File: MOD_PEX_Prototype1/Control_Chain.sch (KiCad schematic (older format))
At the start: 25 parts, among them J1 RJ45_CHAIN_MAIN, J2 RJ45_CHAIN_EXTENSION, Q1 MMBT3904, Q2 MMBT3906, U4 MAX13450E

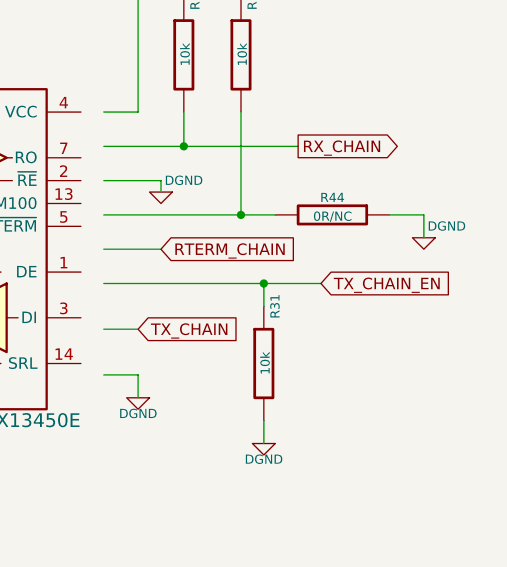
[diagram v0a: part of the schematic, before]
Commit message: Fixing control chain signal names, adding a 0R resistor for the ENABLE_CHAIN signal in the P1 debugging connector and regenerating the netlist.
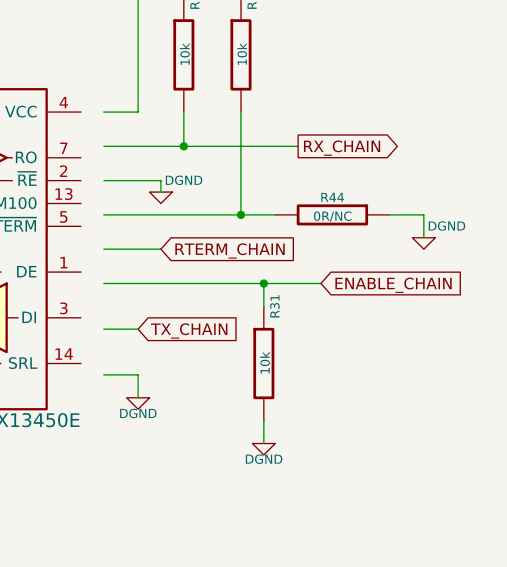
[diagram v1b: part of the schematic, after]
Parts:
- Q1: footprint (none) -> MOD_Footprints_Lib:SOT23
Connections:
- net labels added: ENABLE_CHAIN
- net labels removed: TX_CHAIN_EN
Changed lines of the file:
@@
 $EndComp
 $Comp
-L +3.3V #PWR25
+L +3.3V #PWR028
 U 1 1 548B5A42
 P 1900 2050
-F 0 "#PWR25" H 1900 2010 30  0001 C CNN
+F 0 "#PWR028" H 1900 2010 30  0001 C CNN
 F 1 "+3.3V" H 1900 2160 30  0000 C CNN
 F 2 "" H 1900 2050 60  0000 C CNN
@@
 $EndComp
 $Comp
-L DGND #PWR26
+L DGND #PWR029
 U 1 1 548B5A48
 P 2200 5950
-F 0 "#PWR26" H 2200 5950 40  0001 C CNN
+F 0 "#PWR029" H 2200 5950 40  0001 C CNN
 F 1 "DGND" H 2200 5880 40  0000 C CNN
 F 2 "" H 2200 5950 60  0000 C CNN
@@
 $EndComp
 $Comp
-L DGND #PWR28
+L DGND #PWR030
 U 1 1 548B5A55
 P 2350 4800
-F 0 "#PWR28" H 2350 4800 40  0001 C CNN
+F 0 "#PWR030" H 2350 4800 40  0001 C CNN
 F 1 "DGND" H 2350 4730 40  0000 C CNN
 F 2 "" H 2350 4800 60  0000 C CNN
@@
 RS485_RX-
 $Comp
-L DGND #PWR37
+L DGND #PWR031
 U 1 1 548B5A5E
 P 7250 3250
-F 0 "#PWR37" H 7250 3250 40  0001 C CNN
+F 0 "#PWR031" H 7250 3250 40  0001 C CNN
 F 1 "DGND" H 7250 3150 40  0000 C CNN
 F 2 "" H 7250 3250 60  0000 C CNN
@@
 RX_CHAIN
 Text GLabel 9750 3300 2    50   Input ~ 0
-TX_CHAIN_EN
+ENABLE_CHAIN
 $Comp
 L ZENERsmall D3
@@
 $EndComp
 $Comp
-L DGND #PWR39
+L DGND #PWR032
 U 1 1 548B5A8A
 P 8100 4200
-F 0 "#PWR39" H 8100 4200 40  0001 C CNN
+F 0 "#PWR032" H 8100 4200 40  0001 C CNN
 F 1 "DGND" H 8100 4130 40  0000 C CNN
 F 2 "" H 8100 4200 60  0000 C CNN
@@
 $EndComp
 $Comp
-L DGND #PWR38
+L DGND #PWR033
 U 1 1 548B5A97
 P 7950 5000
-F 0 "#PWR38" H 7950 5000 40  0001 C CNN
+F 0 "#PWR033" H 7950 5000 40  0001 C CNN
 F 1 "DGND" H 7950 4930 40  0000 C CNN
 F 2 "" H 7950 5000 60  0000 C CNN
@@
 PCB consideration: \nThis capacitor must \nbe placed as close as \npossible to the IC
 $Comp
-L +5V #PWR40
+L +5V #PWR034
 U 1 1 548B5A9E
 P 8950 1900
-F 0 "#PWR40" H 8950 1990 20  0001 C CNN
+F 0 "#PWR034" H 8950 1990 20  0001 C CNN
 F 1 "+5V" H 8950 1990 30  0000 C CNN
 F 2 "" H 8950 1900 60  0000 C CNN
@@
 $EndComp
 $Comp
-L DGND #PWR41
+L DGND #PWR035
 U 1 1 548B5AA4
 P 8950 3800
-F 0 "#PWR41" H 8950 3800 40  0001 C CNN
+F 0 "#PWR035" H 8950 3800 40  0001 C CNN
 F 1 "DGND" H 8950 3730 40  0000 C CNN
 F 2 "" H 8950 3800 60  0000 C CNN
@@
 $EndComp
 $Comp
-L DGND #PWR43
+L DGND #PWR036
 U 1 1 548B5AAA
 P 9500 4000
-F 0 "#PWR43" H 9500 4000 40  0001 C CNN
+F 0 "#PWR036" H 9500 4000 40  0001 C CNN
 F 1 "DGND" H 9500 3930 40  0000 C CNN
 F 2 "" H 9500 4000 60  0000 C CNN
@@
 $EndComp
 $Comp
-L DGND #PWR42
+L DGND #PWR037
 U 1 1 548B5AB0
 P 9050 2900
-F 0 "#PWR42" H 9050 2900 40  0001 C CNN
+F 0 "#PWR037" H 9050 2900 40  0001 C CNN
 F 1 "DGND" H 8950 2950 40  0000 C CNN
 F 2 "" H 9050 2900 60  0000 C CNN
@@
 RS485_TX-
 $Comp
-L DGND #PWR27
+L DGND #PWR038
 U 1 1 548B5ABF
 P 2350 3050
-F 0 "#PWR27" H 2350 3050 40  0001 C CNN
+F 0 "#PWR038" H 2350 3050 40  0001 C CNN
 F 1 "DGND" H 2350 2980 40  0000 C CNN
 F 2 "" H 2350 3050 60  0000 C CNN
@@
 $EndComp
 $Comp
-L DGND #PWR44
+L DGND #PWR039
 U 1 1 548B5ACC
 P 10200 3100
-F 0 "#PWR44" H 10200 3100 40  0001 C CNN
+F 0 "#PWR039" H 10200 3100 40  0001 C CNN
 F 1 "DGND" H 10100 3150 40  0000 C CNN
 F 2 "" H 10200 3100 60  0000 C CNN
@@
 RS485_RX-
 $Comp
-L VCC #PWR29
+L VCC #PWR040
 U 1 1 548B5AD6
 P 3600 2450
-F 0 "#PWR29" H 3600 2550 30  0001 C CNN
+F 0 "#PWR040" H 3600 2550 30  0001 C CNN
 F 1 "VCC" H 3600 2550 30  0000 C CNN
 F 2 "" H 3600 2450 60  0000 C CNN
@@
 $EndComp
 $Comp
-L DGND #PWR31
+L DGND #PWR041
 U 1 1 548B5ADC
 P 3600 5950
-F 0 "#PWR31" H 3600 5950 40  0001 C CNN
+F 0 "#PWR041" H 3600 5950 40  0001 C CNN
 F 1 "DGND" H 3600 5880 40  0000 C CNN
 F 2 "" H 3600 5950 60  0000 C CNN
@@
 $EndComp
 $Comp
-L DGND #PWR30
+L DGND #PWR042
 U 1 1 548B5AE2
 P 3600 4200
-F 0 "#PWR30" H 3600 4200 40  0001 C CNN
+F 0 "#PWR042" H 3600 4200 40  0001 C CNN
 F 1 "DGND" H 3600 4130 40  0000 C CNN
 F 2 "" H 3600 4200 60  0000 C CNN
@@
 $EndComp
 $Comp
-L VCC #PWR33
+L VCC #PWR043
 U 1 1 548B5AE8
 P 4000 4750
-F 0 "#PWR33" H 4000 4850 30  0001 C CNN
+F 0 "#PWR043" H 4000 4850 30  0001 C CNN
 F 1 "VCC" H 4000 4850 30  0000 C CNN
 F 2 "" H 4000 4750 60  0000 C CNN
@@
 $EndComp
 $Comp
-L DGND #PWR32
+L DGND #PWR044
 U 1 1 548B5B03
 P 3900 5950
-F 0 "#PWR32" H 3900 5950 40  0001 C CNN
+F 0 "#PWR044" H 3900 5950 40  0001 C CNN
 F 1 "DGND" H 3900 5880 40  0000 C CNN
 F 2 "" H 3900 5950 60  0000 C CNN
@@
 $EndComp
 $Comp
-L DGND #PWR34
+L DGND #PWR045
 U 1 1 548B5B10
 P 4150 5950
-F 0 "#PWR34" H 4150 5950 40  0001 C CNN
+F 0 "#PWR045" H 4150 5950 40  0001 C CNN
 F 1 "DGND" H 4150 5880 40  0000 C CNN
 F 2 "" H 4150 5950 60  0000 C CNN
@@
 RTERM_CHAIN
 $Comp
-L +5V #PWR35
+L +5V #PWR046
 U 1 1 548B5B2D
 P 4900 4300
-F 0 "#PWR35" H 4900 4390 20  0001 C CNN
+F 0 "#PWR046" H 4900 4390 20  0001 C CNN
 F 1 "+5V" H 4900 4390 30  0000 C CNN
 F 2 "" H 4900 4300 60  0000 C CNN
@@
 Connection ~ 3600 3050
 $Comp
-L DGND #PWR36
+L DGND #PWR047
 U 1 1 548B5B99
 P 5950 6100
-F 0 "#PWR36" H 5950 6100 40  0001 C CNN
+F 0 "#PWR047" H 5950 6100 40  0001 C CNN
 F 1 "DGND" H 5950 6030 40  0000 C CNN
 F 2 "" H 5950 6100 60  0000 C CNN
@@
 F 0 "Q1" H 2100 5500 50  0000 R CNN
 F 1 "MMBT3904" V 2300 5850 50  0000 R CNN
-F 2 "" H 2100 5650 60  0000 C CNN
+F 2 "MOD_Footprints_Lib:SOT23" H 2100 5650 60  0001 C CNN
 F 3 "" H 2100 5650 60  0000 C CNN
 	1    2100 5650

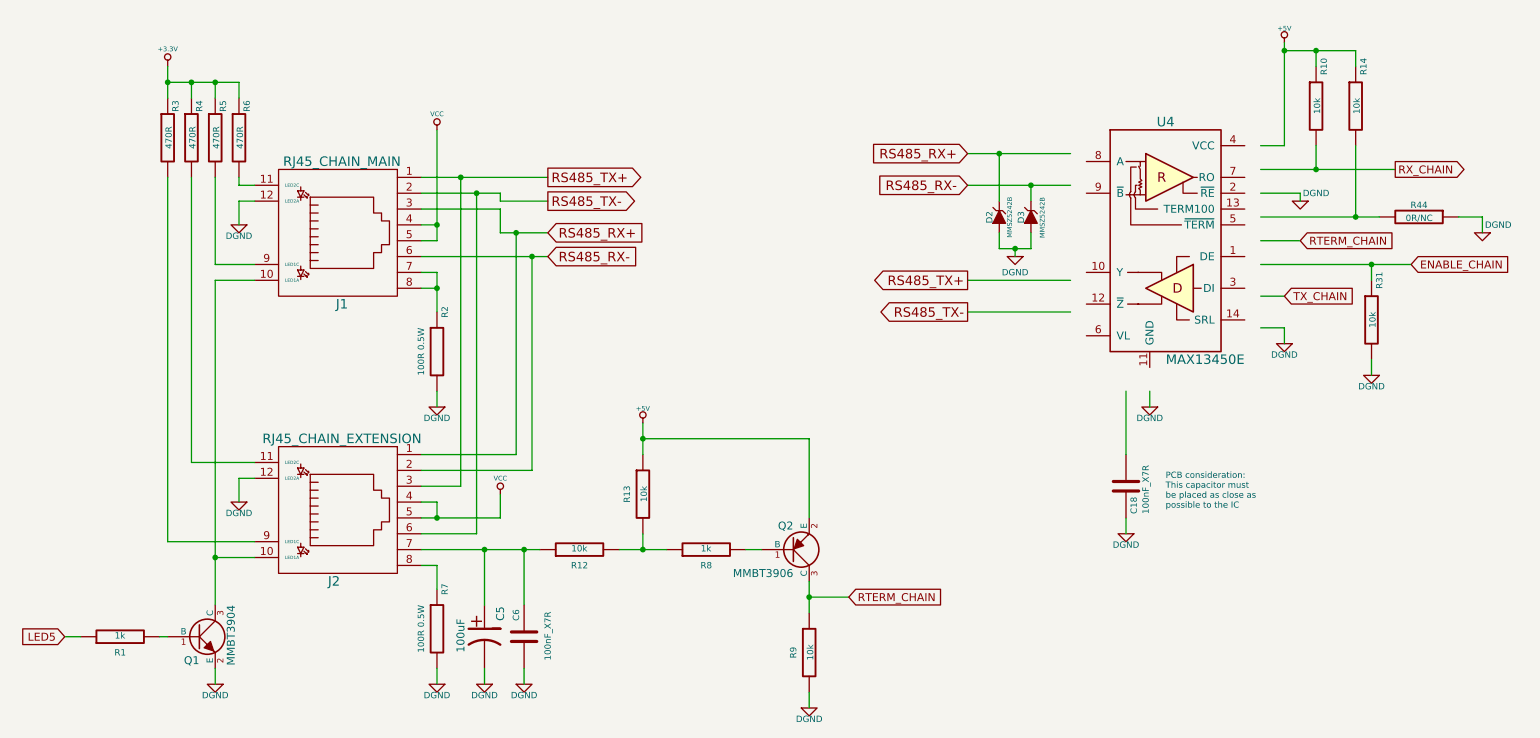
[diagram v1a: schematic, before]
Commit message: wip issue #12: Use 3.3V for Lv in the control chain circuit
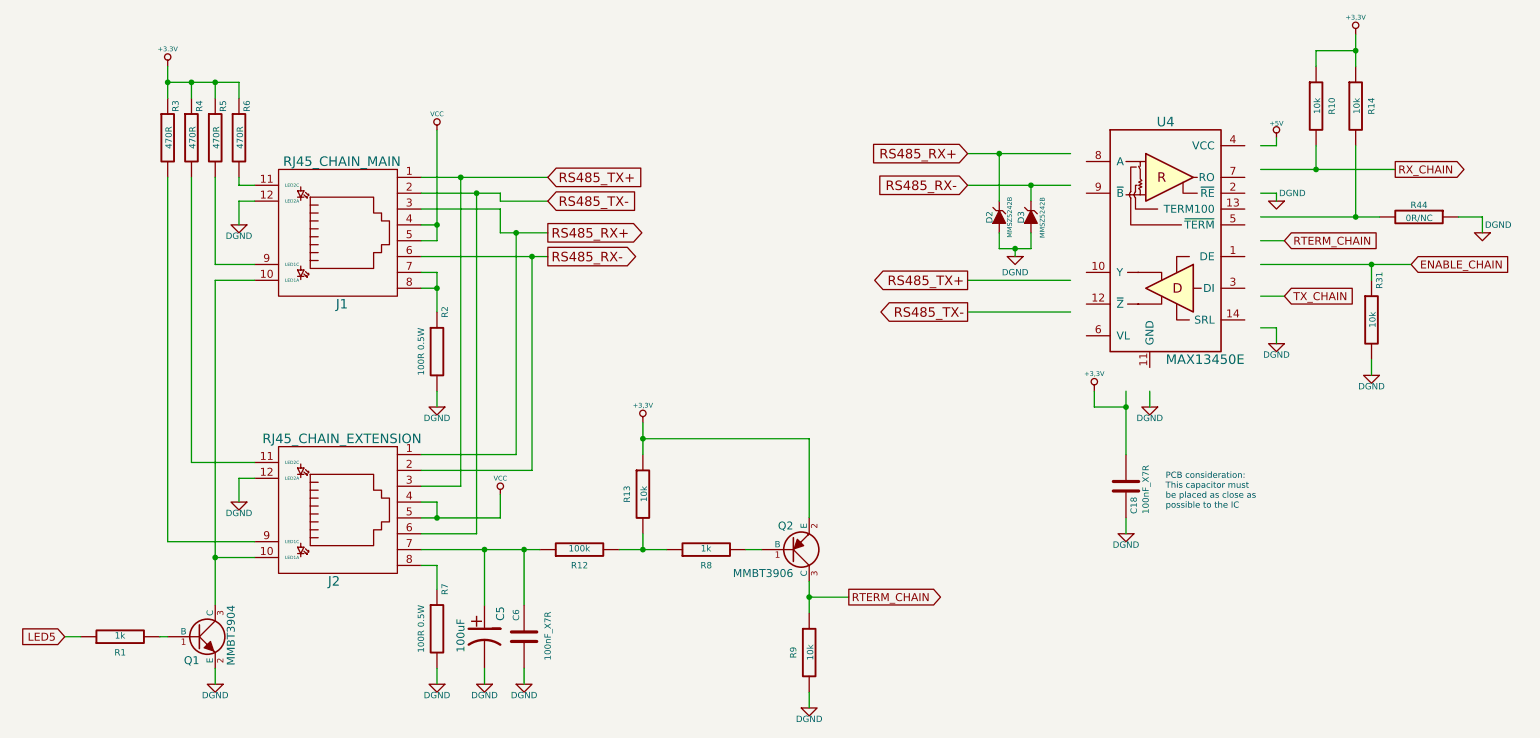
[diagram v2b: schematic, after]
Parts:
- R12: value 10k -> 100k
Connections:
- net labels added: +3,3V
- wire segments 100 -> 102
